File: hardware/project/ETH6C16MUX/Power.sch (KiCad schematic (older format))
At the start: 35 parts

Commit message: Schematic design
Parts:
- removed C? (x2): 330p/2kV, symbol Device:C
- removed L?: 7448014501, symbol ETH6C12MUX:7448014501
- removed R? (x2): NC, symbol Device:R
- removed U?: THL15-2411WI, symbol ETH6C12MUX:THL_15-2411WI
- added C?: 22u, symbol Device:C
- added R?: R, symbol Device:R
- added R?: 1k47, symbol Device:R
- added R?: 2, symbol Device:R
- added U?: OKI-T3-W40P-C, symbol ETH6C16MUX:OKI-T3-W40P-C
- C? (x2): value 4u7/50V -> 22u/50V
- U?: symbol ETH6C12MUX:MAX5902 -> ETH6C16MUX:MAX5902
- U?: symbol ETH6C12MUX:ADP7156ARDZ-3.3-R7 -> ETH6C16MUX:ADP7156ARDZ-3.3-R7
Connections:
- net labels added: +24V
- net labels removed: +24V_PWR, GNDPWR
- wire segments 139 -> 123
- no-connect marks 2 -> 1
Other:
- moved on the sheet: C?, D?, F?, Q?, R?

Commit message: USB update
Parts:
- added FB?: Ferrite_Bead, symbol Device:Ferrite_Bead
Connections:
- net labels added: +5V_USB
- wire segments 123 -> 126
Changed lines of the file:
@@
 Wire Wire Line
 	8800 1450 9350 1450
-Connection ~ 9350 1450
 Wire Wire Line
 	8850 2500 9350 2500
@@
 	550  550  11150 550
 Wire Wire Line
-	9350 1350 9350 1450
+	10300 1350 10300 1450
 $Comp
 L power:+5V #PWR?
 U 1 1 5D730DF9
-P 9350 1350
-F 0 "#PWR?" H 9350 1200 50  0001 C CNN
-F 1 "+5V" H 9365 1523 50  0000 C CNN
-F 2 "" H 9350 1350 50  0001 C CNN
-F 3 "" H 9350 1350 50  0001 C CNN
-	1    9350 1350
+P 10300 1350
+F 0 "#PWR?" H 10300 1200 50  0001 C CNN
+F 1 "+5V" H 10315 1523 50  0000 C CNN
+F 2 "" H 10300 1350 50  0001 C CNN
+F 3 "" H 10300 1350 50  0001 C CNN
+	1    10300 1350
 	1    0    0    -1
 $EndComp
@@
 	1    0    0    -1
 $EndComp
+$Comp
+L Device:Ferrite_Bead FB?
+U 1 1 5D7A9156
+P 9750 1450
+F 0 "FB?" V 9476 1450 50  0000 C CNN
+F 1 "Ferrite_Bead" V 9567 1450 50  0000 C CNN
+F 2 "" V 9680 1450 50  0001 C CNN
+F 3 "~" H 9750 1450 50  0001 C CNN
+	1    9750 1450
+	0    1    1    0
+$EndComp
+Wire Wire Line
+	9600 1450 9350 1450
+Connection ~ 9350 1450
+Wire Wire Line
+	9900 1450 10300 1450
+$Comp
+L ETH6C16MUX:+5V_USB #PWR?
+U 1 1 5D7BEAC4
+P 5100 7000
+F 0 "#PWR?" H 5100 6850 50  0001 C CNN
+F 1 "+5V_USB" H 5115 7173 50  0000 C CNN
+F 2 "" H 5100 7000 50  0001 C CNN
+F 3 "" H 5100 7000 50  0001 C CNN
+	1    5100 7000
+	1    0    0    -1
+$EndComp
+$Comp
+L power:PWR_FLAG #FLG?
+U 1 1 5D7BF332
+P 5100 7150
+F 0 "#FLG?" H 5100 7225 50  0001 C CNN
+F 1 "PWR_FLAG" H 5100 7323 50  0000 C CNN
+F 2 "" H 5100 7150 50  0001 C CNN
+F 3 "~" H 5100 7150 50  0001 C CNN
+	1    5100 7150
+	-1   0    0    1
+$EndComp
+Wire Wire Line
+	5100 7000 5100 7150
 $EndSCHEMATC

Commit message: FPGA schematic
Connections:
- net labels added: +1.2V_FPGA_VCC, +1.2V_PLL_VCC, +2.5V_FPGA_VCC
- net labels removed: FPGA_VCC_1V2, FPGA_VCC_2V5, PLL_VCC_1V2
- wire segments 126 -> 127
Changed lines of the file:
@@
 	8750 5200 8750 5300
 Connection ~ 8750 5300
-$Comp
-L ETH6C16MUX:PLL_VCC_1V2 #PWR?
-U 1 1 5D7C14AE
-P 10000 3950
-F 0 "#PWR?" H 10000 3800 50  0001 C CNN
-F 1 "PLL_VCC_1V2" H 10015 4123 50  0000 C CNN
-F 2 "" H 10000 3950 50  0001 C CNN
-F 3 "" H 10000 3950 50  0001 C CNN
-	1    10000 3950
-	1    0    0    -1
-$EndComp
 Wire Wire Line
 	10000 3950 10000 4050
 Connection ~ 10000 4050
-$Comp
-L ETH6C16MUX:FPGA_VCC_1V2 #PWR?
-U 1 1 5D7CC31B
-P 8750 3950
-F 0 "#PWR?" H 8750 3800 50  0001 C CNN
-F 1 "FPGA_VCC_1V2" H 8765 4123 50  0000 C CNN
-F 2 "" H 8750 3950 50  0001 C CNN
-F 3 "" H 8750 3950 50  0001 C CNN
-	1    8750 3950
-	1    0    0    -1
-$EndComp
 Wire Wire Line
 	8750 3950 8750 4050
@@
 Wire Wire Line
 	9500 4050 10000 4050
-$Comp
-L ETH6C16MUX:FPGA_VCC_2V5 #PWR?
-U 1 1 5D7E5EEF
-P 8750 5200
-F 0 "#PWR?" H 8750 5050 50  0001 C CNN
-F 1 "FPGA_VCC_2V5" H 8765 5373 50  0000 C CNN
-F 2 "" H 8750 5200 50  0001 C CNN
-F 3 "" H 8750 5200 50  0001 C CNN
-	1    8750 5200
-	1    0    0    -1
-$EndComp
 $Comp
 L ETH6C16MUX:ADP7156ARDZ-3.3-R7 U?
@@
 	1    0    0    -1
 $EndComp
-$Comp
-L ETH6C16MUX:PLL_VCC_1V2 #PWR?
-U 1 1 5D94775A
-P 3400 7000
-F 0 "#PWR?" H 3400 6850 50  0001 C CNN
-F 1 "PLL_VCC_1V2" H 3415 7173 50  0000 C CNN
-F 2 "" H 3400 7000 50  0001 C CNN
-F 3 "" H 3400 7000 50  0001 C CNN
-	1    3400 7000
-	1    0    0    -1
-$EndComp
-$Comp
-L ETH6C16MUX:FPGA_VCC_2V5 #PWR?
-U 1 1 5D94EEDF
-P 4000 7000
-F 0 "#PWR?" H 4000 6850 50  0001 C CNN
-F 1 "FPGA_VCC_2V5" H 4015 7173 50  0000 C CNN
-F 2 "" H 4000 7000 50  0001 C CNN
-F 3 "" H 4000 7000 50  0001 C CNN
-	1    4000 7000
-	1    0    0    -1
-$EndComp
 Wire Wire Line
 	2250 7000 2250 7150
@@
 L power:PWR_FLAG #FLG?
 U 1 1 5D97811F
-P 3400 7150
-F 0 "#FLG?" H 3400 7225 50  0001 C CNN
-F 1 "PWR_FLAG" H 3400 7323 50  0000 C CNN
-F 2 "" H 3400 7150 50  0001 C CNN
-F 3 "~" H 3400 7150 50  0001 C CNN
-	1    3400 7150
+P 3450 7150
+F 0 "#FLG?" H 3450 7225 50  0001 C CNN
+F 1 "PWR_FLAG" H 3450 7323 50  0000 C CNN
+F 2 "" H 3450 7150 50  0001 C CNN
+F 3 "~" H 3450 7150 50  0001 C CNN
+	1    3450 7150
 	-1   0    0    1
 $EndComp
 Wire Wire Line
-	3400 7000 3400 7150
+	3450 7000 3450 7150
 $Comp
 L power:PWR_FLAG #FLG?
 U 1 1 5D9981B5
-P 4000 7150
-F 0 "#FLG?" H 4000 7225 50  0001 C CNN
-F 1 "PWR_FLAG" H 4000 7323 50  0000 C CNN
-F 2 "" H 4000 7150 50  0001 C CNN
-F 3 "~" H 4000 7150 50  0001 C CNN
-	1    4000 7150
+P 4150 7150
+F 0 "#FLG?" H 4150 7225 50  0001 C CNN
+F 1 "PWR_FLAG" H 4150 7323 50  0000 C CNN
+F 2 "" H 4150 7150 50  0001 C CNN
+F 3 "~" H 4150 7150 50  0001 C CNN
+	1    4150 7150
 	-1   0    0    1
 $EndComp
 Wire Wire Line
-	4000 7000 4000 7150
+	4150 7000 4150 7150
 $Comp
 L power:+5V #PWR?
 U 1 1 5D9B1EAC
-P 4550 7000
-F 0 "#PWR?" H 4550 6850 50  0001 C CNN
-F 1 "+5V" H 4565 7173 50  0000 C CNN
-F 2 "" H 4550 7000 50  0001 C CNN
-F 3 "" H 4550 7000 50  0001 C CNN
-	1    4550 7000
+P 4700 7000
+F 0 "#PWR?" H 4700 6850 50  0001 C CNN
+F 1 "+5V" H 4715 7173 50  0000 C CNN
+F 2 "" H 4700 7000 50  0001 C CNN
+F 3 "" H 4700 7000 50  0001 C CNN
+	1    4700 7000
 	1    0    0    -1
 $EndComp
@@
 L power:PWR_FLAG #FLG?
 U 1 1 5D9B2CC2
-P 4550 7150
-F 0 "#FLG?" H 4550 7225 50  0001 C CNN
-F 1 "PWR_FLAG" H 4550 7323 50  0000 C CNN
-F 2 "" H 4550 7150 50  0001 C CNN
-F 3 "~" H 4550 7150 50  0001 C CNN
-	1    4550 7150
+P 4700 7150
+F 0 "#FLG?" H 4700 7225 50  0001 C CNN
+F 1 "PWR_FLAG" H 4700 7323 50  0000 C CNN
+F 2 "" H 4700 7150 50  0001 C CNN
+F 3 "~" H 4700 7150 50  0001 C CNN
+	1    4700 7150
 	-1   0    0    1
 $EndComp
 Wire Wire Line
-	4550 7150 4550 7000
+	4700 7150 4700 7000
 Wire Wire Line
 	2500 4950 2500 4800
@@
 L ETH6C16MUX:+5V_USB #PWR?
 U 1 1 5D7BEAC4
-P 5100 7000
-F 0 "#PWR?" H 5100 6850 50  0001 C CNN
-F 1 "+5V_USB" H 5115 7173 50  0000 C CNN
-F 2 "" H 5100 7000 50  0001 C CNN
-F 3 "" H 5100 7000 50  0001 C CNN
-	1    5100 7000
+P 5250 7000
+F 0 "#PWR?" H 5250 6850 50  0001 C CNN
+F 1 "+5V_USB" H 5265 7173 50  0000 C CNN
+F 2 "" H 5250 7000 50  0001 C CNN
+F 3 "" H 5250 7000 50  0001 C CNN
+	1    5250 7000
 	1    0    0    -1
 $EndComp
@@
 L power:PWR_FLAG #FLG?
 U 1 1 5D7BF332
-P 5100 7150
-F 0 "#FLG?" H 5100 7225 50  0001 C CNN
-F 1 "PWR_FLAG" H 5100 7323 50  0000 C CNN
-F 2 "" H 5100 7150 50  0001 C CNN
-F 3 "~" H 5100 7150 50  0001 C CNN
-	1    5100 7150
+P 5250 7150
+F 0 "#FLG?" H 5250 7225 50  0001 C CNN
+F 1 "PWR_FLAG" H 5250 7323 50  0000 C CNN
+F 2 "" H 5250 7150 50  0001 C CNN
+F 3 "~" H 5250 7150 50  0001 C CNN
+	1    5250 7150
 	-1   0    0    1
 $EndComp
 Wire Wire Line
-	5100 7000 5100 7150
+	5250 7000 5250 7150
+$Comp
+L ETH6C16MUX:+1.2V_FPGA_VCC #PWR?
+U 1 1 5DD5449E
+P 8750 3950
+F 0 "#PWR?" H 8750 3800 50  0001 C CNN
+F 1 "+1.2V_FPGA_VCC" H 8765 4123 50  0000 C CNN
+F 2 "" H 8750 3950 50  0001 C CNN
+F 3 "" H 8750 3950 50  0001 C CNN
+	1    8750 3950
+	1    0    0    -1
+$EndComp
+$Comp
+L ETH6C16MUX:+1.2V_PLL_VCC #PWR?
+U 1 1 5DD5D580
+P 10000 3950
+F 0 "#PWR?" H 10000 3800 50  0001 C CNN
+F 1 "+1.2V_PLL_VCC" H 10015 4123 50  0000 C CNN
+F 2 "" H 10000 3950 50  0001 C CNN
+F 3 "" H 10000 3950 50  0001 C CNN
+	1    10000 3950
+	1    0    0    -1
+$EndComp
+$Comp
+L ETH6C16MUX:+2.5V_FPGA_VCC #PWR?
+U 1 1 5DD5E81C
+P 8750 5200
+F 0 "#PWR?" H 8750 5050 50  0001 C CNN
+F 1 "+2.5V_FPGA_VCC" H 8765 5373 50  0000 C CNN
+F 2 "" H 8750 5200 50  0001 C CNN
+F 3 "" H 8750 5200 50  0001 C CNN
+	1    8750 5200
+	1    0    0    -1
+$EndComp
+$Comp
+L ETH6C16MUX:+2.5V_FPGA_VCC #PWR?
+U 1 1 5DD64D64
+P 3450 7000
+F 0 "#PWR?" H 3450 6850 50  0001 C CNN
+F 1 "+2.5V_FPGA_VCC" H 3465 7173 50  0000 C CNN
+F 2 "" H 3450 7000 50  0001 C CNN
+F 3 "" H 3450 7000 50  0001 C CNN
+	1    3450 7000
+	1    0    0    -1
+$EndComp
+$Comp
+L ETH6C16MUX:+1.2V_PLL_VCC #PWR?
+U 1 1 5DD67504
+P 4150 7000
+F 0 "#PWR?" H 4150 6850 50  0001 C CNN
+F 1 "+1.2V_PLL_VCC" H 4165 7173 50  0000 C CNN
+F 2 "" H 4150 7000 50  0001 C CNN
+F 3 "" H 4150 7000 50  0001 C CNN
+	1    4150 7000
+	1    0    0    -1
+$EndComp
+$Comp
+L ETH6C16MUX:+1.2V_FPGA_VCC #PWR?
+U 1 1 5DD86333
+P 5850 7000
+F 0 "#PWR?" H 5850 6850 50  0001 C CNN
+F 1 "+1.2V_FPGA_VCC" H 5865 7173 50  0000 C CNN
+F 2 "" H 5850 7000 50  0001 C CNN
+F 3 "" H 5850 7000 50  0001 C CNN
+	1    5850 7000
+	1    0    0    -1
+$EndComp
+$Comp
+L power:PWR_FLAG #FLG?
+U 1 1 5DD868EC
+P 5850 7150
+F 0 "#FLG?" H 5850 7225 50  0001 C CNN
+F 1 "PWR_FLAG" H 5850 7323 50  0000 C CNN
+F 2 "" H 5850 7150 50  0001 C CNN
+F 3 "~" H 5850 7150 50  0001 C CNN
+	1    5850 7150
+	-1   0    0    1
+$EndComp
+Wire Wire Line
+	5850 7150 5850 7000
 $EndSCHEMATC

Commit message: Schematic design
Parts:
- removed C? (x3): 22u, symbol Device:C
- removed C? (x2): 100n, symbol Device:C
- removed R?: 120, symbol Device:R
- removed R?: 10, symbol Device:R
- removed U?: LD1117S25TR_SOT223, Package_TO_SOT_SMD:SOT-223-3_TabPin2, symbol Regulator_Linear:LD1117S25TR_SOT223
- D703: renamed from D?; footprint (none) -> LED_SMD:LED_0603_1608Metric_Pad1.05x0.95mm_HandSolder
- F701: renamed from F?; value MF-LSMF185/33X -> Ferrite
- FB701: renamed from FB?; value Ferrite_Bead -> 742792031
- U701: renamed from U?; footprint (none) -> ETH6C16MXU:OKI-T3-W40
- gave numbers to parts that had none: 23
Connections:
- net labels added: +3.3V, Earth
- net labels removed: +1.2V_PLL_VCC, +3.3V_FPGA, +3.3V_MCU, +5V_USB
- wire segments 127 -> 99
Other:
- note added: "FPGA +1.2V\n"
- note removed: "FPGA +1.2V and +2.5V"

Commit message: PCB design, need to redesign of the board to board connectors.
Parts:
- removed L701: 744053220, symbol Device:L
- added FB702: 742792031, ETH6C16MXU:R_0805_D_Pad1.15x1.40mm_HandSolder, symbol Device:Ferrite_Bead
- C701, C702: footprint (none) -> Capacitor_SMD:C_2220_5650Metric_Pad1.97x5.40mm_HandSolder
- C703, C704, C705, C706, C707: footprint (none) -> ETH6C16MXU:C_1210_BB_3225Metric_Pad1.42x2.65mm_HandSolder
- C708, C709, C710: footprint (none) -> ETH6C16MXU:C_0805_C_Pad1.15x1.40mm_HandSolder
- D701: value D_Zener -> MMSZ5249B-E3-18; footprint (none) -> Diode_SMD:D_SOD-123
- D702: footprint (none) -> ETH6C16MXU:DO_214AA_REV
- F701: value Ferrite -> MF-LSMF185/33X; footprint (none) -> ETH6C16MXU:Fuse_SMD2920
- FB701: footprint (none) -> ETH6C16MXU:R_0805_D_Pad1.15x1.40mm_HandSolder
- Q701: footprint (none) -> ETH6C16MXU:TO-252-2_Rectifier
- R701, R702, R705, R706: footprint (none) -> Resistor_SMD:R_0603_1608Metric_Pad1.05x0.95mm_HandSolder
- R703: value R -> 6k8/0.5W; footprint (none) -> Resistor_SMD:R_0805_2012Metric_Pad1.15x1.40mm_HandSolder
- R704: value R -> 370; footprint (none) -> Resistor_SMD:R_0603_1608Metric_Pad1.05x0.95mm_HandSolder
- U702: footprint (none) -> Package_TO_SOT_SMD:SOT-23-6_Handsoldering
- U704: footprint (none) -> Package_SO:SOIC-8-1EP_3.9x4.9mm_P1.27mm_EP2.41x3.81mm_ThermalVias
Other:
- moved on the sheet: C704, C705, D701, D702, D703, F701, Q701, R702, R703, R704, U702, U703

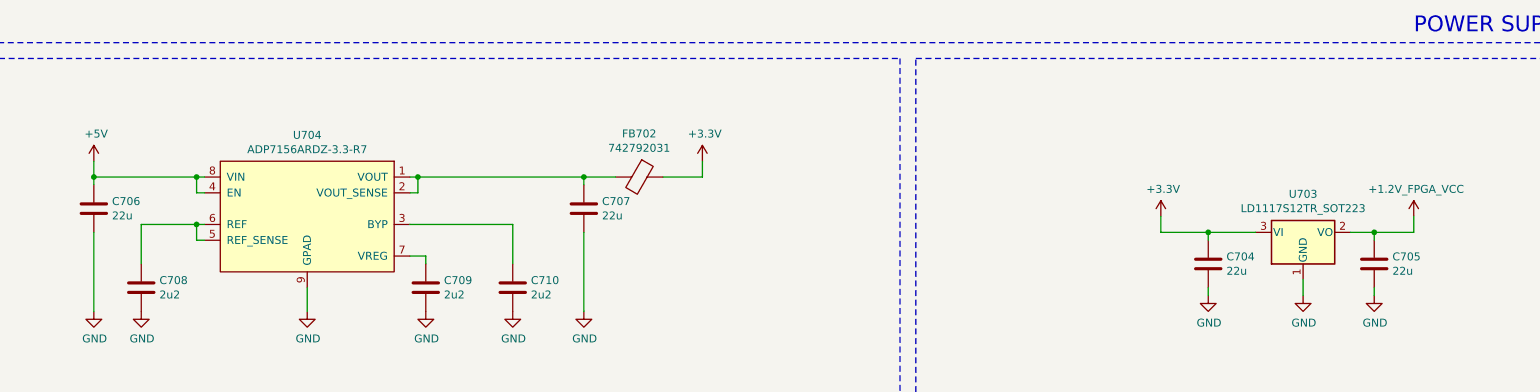
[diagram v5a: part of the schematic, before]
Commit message: PCB layout, board to board connector changed.
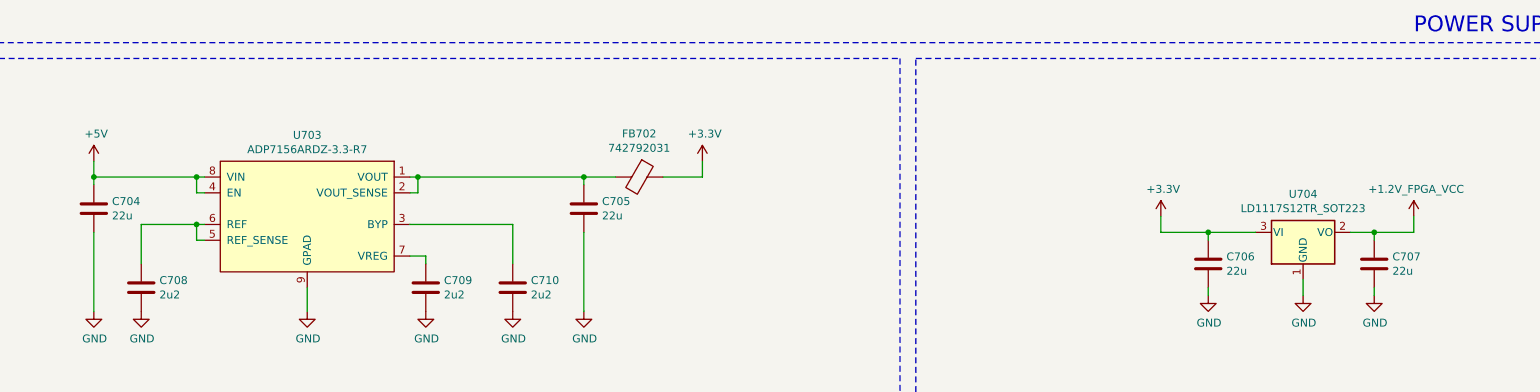
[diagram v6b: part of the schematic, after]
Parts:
- renumbered C706 to C704, C707 to C705, C704 to C706, C705 to C707, U704 to U703, U703 to U704
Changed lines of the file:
@@
 $Descr A4 11693 8268
 encoding utf-8
-Sheet 7 9
+Sheet 7 8
 Title ""
 Date ""
@@
 $EndDescr
 $Comp
-L ETH6C16MUX:ADP7156ARDZ-3.3-R7 U704
+L ETH6C16MUX:ADP7156ARDZ-3.3-R7 U703
 U 1 1 5D7F7326
 P 2500 4350
-F 0 "U704" H 2500 4865 50  0000 C CNN
+F 0 "U703" H 2500 4865 50  0000 C CNN
 F 1 "ADP7156ARDZ-3.3-R7" H 2500 4774 50  0000 C CNN
 F 2 "Package_SO:SOIC-8-1EP_3.9x4.9mm_P1.27mm_EP2.41x3.81mm_ThermalVias" H 2500 4800 50  0001 C CNN
@@
 	1800 4100 1850 4100
 $Comp
-L Device:C C706
+L Device:C C704
 U 1 1 5D81B4F1
 P 1150 4300
-F 0 "C706" H 1265 4346 50  0000 L CNN
+F 0 "C704" H 1265 4346 50  0000 L CNN
 F 1 "22u" H 1265 4255 50  0000 L CNN
 F 2 "ETH6C16MXU:C_1210_BB_3225Metric_Pad1.42x2.65mm_HandSolder" H 1188 4150 50  0001 C CNN
@@
 $EndComp
 $Comp
-L power:+5V #PWR0709
+L power:+5V #PWR0704
 U 1 1 5D81FACA
 P 1150 4000
-F 0 "#PWR0709" H 1150 3850 50  0001 C CNN
+F 0 "#PWR0704" H 1150 3850 50  0001 C CNN
 F 1 "+5V" H 1165 4173 50  0000 C CNN
 F 2 "" H 1150 4000 50  0001 C CNN
@@
 Connection ~ 1800 4400
 $Comp
-L power:GND #PWR0715
+L power:GND #PWR0713
 U 1 1 5D842B2C
 P 2500 4950
-F 0 "#PWR0715" H 2500 4700 50  0001 C CNN
+F 0 "#PWR0713" H 2500 4700 50  0001 C CNN
 F 1 "GND" H 2505 4777 50  0000 C CNN
 F 2 "" H 2500 4950 50  0001 C CNN
@@
 $EndComp
 $Comp
-L power:GND #PWR0714
+L power:GND #PWR0712
 U 1 1 5D842E25
 P 1450 4950
-F 0 "#PWR0714" H 1450 4700 50  0001 C CNN
+F 0 "#PWR0712" H 1450 4700 50  0001 C CNN
 F 1 "GND" H 1455 4777 50  0000 C CNN
 F 2 "" H 1450 4950 50  0001 C CNN
@@
 $EndComp
 $Comp
-L power:GND #PWR0713
+L power:GND #PWR0711
 U 1 1 5D846739
 P 1150 4950
-F 0 "#PWR0713" H 1150 4700 50  0001 C CNN
+F 0 "#PWR0711" H 1150 4700 50  0001 C CNN
 F 1 "GND" H 1155 4777 50  0000 C CNN
 F 2 "" H 1150 4950 50  0001 C CNN
@@
 	3800 4400 3150 4400
 $Comp
-L power:GND #PWR0716
+L power:GND #PWR0714
 U 1 1 5D85848D
 P 3250 4950
-F 0 "#PWR0716" H 3250 4700 50  0001 C CNN
+F 0 "#PWR0714" H 3250 4700 50  0001 C CNN
 F 1 "GND" H 3255 4777 50  0000 C CNN
 F 2 "" H 3250 4950 50  0001 C CNN
@@
 $EndComp
 $Comp
-L power:GND #PWR0717
+L power:GND #PWR0715
 U 1 1 5D85872F
 P 3800 4950
-F 0 "#PWR0717" H 3800 4700 50  0001 C CNN
+F 0 "#PWR0715" H 3800 4700 50  0001 C CNN
 F 1 "GND" H 3805 4777 50  0000 C CNN
 F 2 "" H 3800 4950 50  0001 C CNN
@@
 	1150 4100 1150 4150
 $Comp
-L Device:C C707
+L Device:C C705
 U 1 1 5D8779F6
 P 4250 4300
-F 0 "C707" H 4365 4346 50  0000 L CNN
+F 0 "C705" H 4365 4346 50  0000 L CNN
 F 1 "22u" H 4365 4255 50  0000 L CNN
 F 2 "ETH6C16MXU:C_1210_BB_3225Metric_Pad1.42x2.65mm_HandSolder" H 4288 4150 50  0001 C CNN
@@
 $EndComp
 $Comp
-L power:GND #PWR0718
+L power:GND #PWR0716
 U 1 1 5D8779FC
 P 4250 4950
-F 0 "#PWR0718" H 4250 4700 50  0001 C CNN
+F 0 "#PWR0716" H 4250 4700 50  0001 C CNN
 F 1 "GND" H 4255 4777 50  0000 C CNN
 F 2 "" H 4250 4950 50  0001 C CNN
@@
 	5000 4100 4750 4100
 $Comp
-L power:PWR_FLAG #FLG0702
+L power:PWR_FLAG #FLG0703
 U 1 1 5D8EFE08
 P 800 7150
-F 0 "#FLG0702" H 800 7225 50  0001 C CNN
+F 0 "#FLG0703" H 800 7225 50  0001 C CNN
 F 1 "PWR_FLAG" H 800 7323 50  0000 C CNN
 F 2 "" H 800 7150 50  0001 C CNN
@@
 $EndComp
 $Comp
-L power:GND #PWR0727
+L power:GND #PWR0721
 U 1 1 5D9353CB
 P 1350 7150
-F 0 "#PWR0727" H 1350 6900 50  0001 C CNN
+F 0 "#PWR0721" H 1350 6900 50  0001 C CNN
 F 1 "GND" H 1355 6977 50  0000 C CNN
 F 2 "" H 1350 7150 50  0001 C CNN
@@
 	1350 7150 1350 7000
 $Comp
-L power:PWR_FLAG #FLG0703
+L power:PWR_FLAG #FLG0704
 U 1 1 5D93BEDF
 P 1900 7150
-F 0 "#FLG0703" H 1900 7225 50  0001 C CNN
+F 0 "#FLG0704" H 1900 7225 50  0001 C CNN
 F 1 "PWR_FLAG" H 1900 7323 50  0000 C CNN
 F 2 "" H 1900 7150 50  0001 C CNN
@@
 	2500 7000 2500 7150
 $Comp
-L power:+5V #PWR0724
+L power:+5V #PWR0720
 U 1 1 5D9B1EAC
 P 3100 7000
-F 0 "#PWR0724" H 3100 6850 50  0001 C CNN
+F 0 "#PWR0720" H 3100 6850 50  0001 C CNN
 F 1 "+5V" H 3115 7173 50  0000 C CNN
 F 2 "" H 3100 7000 50  0001 C CNN
@@
 $EndComp
 $Comp
-L power:PWR_FLAG #FLG0707
+L power:PWR_FLAG #FLG0706
 U 1 1 5D9B2CC2
 P 3100 7150
-F 0 "#FLG0707" H 3100 7225 50  0001 C CNN
+F 0 "#FLG0706" H 3100 7225 50  0001 C CNN
 F 1 "PWR_FLAG" H 3100 7323 50  0000 C CNN
 F 2 "" H 3100 7150 50  0001 C CNN
@@
 $EndComp
 $Comp
-L power:+24V #PWR0719
+L power:+24V #PWR0717
 U 1 1 5D7B52AE
 P 800 7000
-F 0 "#PWR0719" H 800 6850 50  0001 C CNN
+F 0 "#PWR0717" H 800 6850 50  0001 C CNN
 F 1 "+24V" H 815 7173 50  0000 C CNN
 F 2 "" H 800 7000 50  0001 C CNN
@@
 $EndComp
 $Comp
-L ETH6C16MUX:+2.5V_FPGA_VCC #PWR0722
+L ETH6C16MUX:+2.5V_FPGA_VCC #PWR0719
 U 1 1 5DD64D64
 P 2500 7000
-F 0 "#PWR0722" H 2500 6850 50  0001 C CNN
+F 0 "#PWR0719" H 2500 6850 50  0001 C CNN
 F 1 "+2.5V_FPGA_VCC" H 2515 7173 50  0000 C CNN
 F 2 "" H 2500 7000 50  0001 C CNN
@@
 	9250 4850 9250 4800
 $Comp
-L power:GND #PWR0712
+L power:GND #PWR0710
 U 1 1 5D75360B
 P 9250 4850
-F 0 "#PWR0712" H 9250 4600 50  0001 C CNN
+F 0 "#PWR0710" H 9250 4600 50  0001 C CNN
 F 1 "GND" H 9255 4677 50  0000 C CNN
 F 2 "" H 9250 4850 50  0001 C CNN
@@
 	9250 4500 9250 4450
 $Comp
-L Device:C C705
+L Device:C C707
 U 1 1 5D7513D7
 P 9250 4650
-F 0 "C705" H 9365 4696 50  0000 L CNN
+F 0 "C707" H 9365 4696 50  0000 L CNN
 F 1 "22u" H 9365 4605 50  0000 L CNN
 F 2 "ETH6C16MXU:C_1210_BB_3225Metric_Pad1.42x2.65mm_HandSolder" H 9288 4500 50  0001 C CNN
@@
 	8800 4850 8800 4750
 $Comp
-L power:GND #PWR0710
+L power:GND #PWR0708
 U 1 1 5D74BF9C
 P 8200 4850
-F 0 "#PWR0710" H 8200 4600 50  0001 C CNN
+F 0 "#PWR0708" H 8200 4600 50  0001 C CNN
 F 1 "GND" H 8205 4677 50  0000 C CNN
 F 2 "" H 8200 4850 50  0001 C CNN
@@
 	8500 4450 8200 4450
 $Comp
-L Device:C C704
+L Device:C C706
 U 1 1 5D748AA0
 P 8200 4650
-F 0 "C704" H 8315 4696 50  0000 L CNN
+F 0 "C706" H 8315 4696 50  0000 L CNN
 F 1 "22u" H 8315 4605 50  0000 L CNN
 F 2 "ETH6C16MXU:C_1210_BB_3225Metric_Pad1.42x2.65mm_HandSolder" H 8238 4500 50  0001 C CNN
@@
 $EndComp
 $Comp
-L power:GND #PWR0711
+L power:GND #PWR0709
 U 1 1 5D742B25
 P 8800 4850
-F 0 "#PWR0711" H 8800 4600 50  0001 C CNN
+F 0 "#PWR0709" H 8800 4600 50  0001 C CNN
 F 1 "GND" H 8805 4677 50  0000 C CNN
 F 2 "" H 8800 4850 50  0001 C CNN
@@
 $EndComp
 $Comp
-L Regulator_Linear:LD1117S12TR_SOT223 U703
+L Regulator_Linear:LD1117S12TR_SOT223 U704
 U 1 1 5D73B8A5
 P 8800 4450
-F 0 "U703" H 8800 4692 50  0000 C CNN
+F 0 "U704" H 8800 4692 50  0000 C CNN
 F 1 "LD1117S12TR_SOT223" H 8800 4601 50  0000 C CNN
 F 2 "Package_TO_SOT_SMD:SOT-223-3_TabPin2" H 8800 4650 50  0001 C CNN
@@
 	10300 1350 10300 1450
 $Comp
-L power:PWR_FLAG #FLG0710
+L power:PWR_FLAG #FLG0702
 U 1 1 5DA17DFF
 P 3600 7000
-F 0 "#FLG0710" H 3600 7075 50  0001 C CNN
+F 0 "#FLG0702" H 3600 7075 50  0001 C CNN
 F 1 "PWR_FLAG" H 3600 7173 50  0000 C CNN
 F 2 "" H 3600 7000 50  0001 C CNN
@@
 $EndComp
 $Comp
-L power:Earth #PWR0728
+L power:Earth #PWR0722
 U 1 1 5DA19730
 P 3600 7150
-F 0 "#PWR0728" H 3600 6900 50  0001 C CNN
+F 0 "#PWR0722" H 3600 6900 50  0001 C CNN
 F 1 "Earth" H 3600 7000 50  0001 C CNN
 F 2 "" H 3600 7150 50  0001 C CNN
@@
 	3600 7150 3600 7000
 $Comp
-L power:+3.3V #PWR0130
+L power:+3.3V #PWR0705
 U 1 1 5DA3ED85
 P 5000 4000
-F 0 "#PWR0130" H 5000 3850 50  0001 C CNN
+F 0 "#PWR0705" H 5000 3850 50  0001 C CNN
 F 1 "+3.3V" H 5015 4173 50  0000 C CNN
 F 2 "" H 5000 4000 50  0001 C CNN
@@
 $EndComp
 $Comp
-L power:+3.3V #PWR0131
+L power:+3.3V #PWR0706
 U 1 1 5DA45A0D
 P 7900 4350
-F 0 "#PWR0131" H 7900 4200 50  0001 C CNN
+F 0 "#PWR0706" H 7900 4200 50  0001 C CNN
 F 1 "+3.3V" H 7915 4523 50  0000 C CNN
 F 2 "" H 7900 4350 50  0001 C CNN
@@
 $EndComp
 $Comp
-L power:+3.3V #PWR0132
+L power:+3.3V #PWR0718
 U 1 1 5DA52CAB
 P 1900 7000
-F 0 "#PWR0132" H 1900 6850 50  0001 C CNN
+F 0 "#PWR0718" H 1900 6850 50  0001 C CNN
 F 1 "+3.3V" H 1915 7173 50  0000 C CNN
 F 2 "" H 1900 7000 50  0001 C CNN
